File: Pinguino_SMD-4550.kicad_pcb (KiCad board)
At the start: 2 copper layers, 50.8 x 25 mm, 55 parts, among them P1 uUSB, P10 CONN_01X01, P11 CONN_01X01, P12 CONN_01X01, P13 CONN_01X01, P14 CONN_01X01, P15 CONN_01X01, P16 CONN_01X01, P17 CONN_01X01, P18 CONN_01X01, P19 CONN_01X01, P2 CONN_01X01, P20 CONN_01X01, P21 CONN_01X01, P22 CONN_01X01, P23 CONN_01X01, P24 CONN_01X01, P25 CONN_01X01, P26 CONN_01X01, P27 CONN_01X01, P28 CONN_01X01, P29 CONN_01X01, P3 CONN_01X01, P30 CONN_01X01, P31 CONN_01X01, P32 CONN_01X01, P33 CONN_01X01, P34 CONN_01X01, P35 CONN_01X01, P36 CONN_01X01, P37 CONN_01X01, P38 CONN_01X01, P4 CONN_01X01, P5 CONN_01X01, P6 CONN_01X01, P7 CONN_01X01, P8 CONN_01X01, P9 CONN_01X01, SW1 Reset, U1 PIC18(L)F4550-I/PT, Y1 Crystal

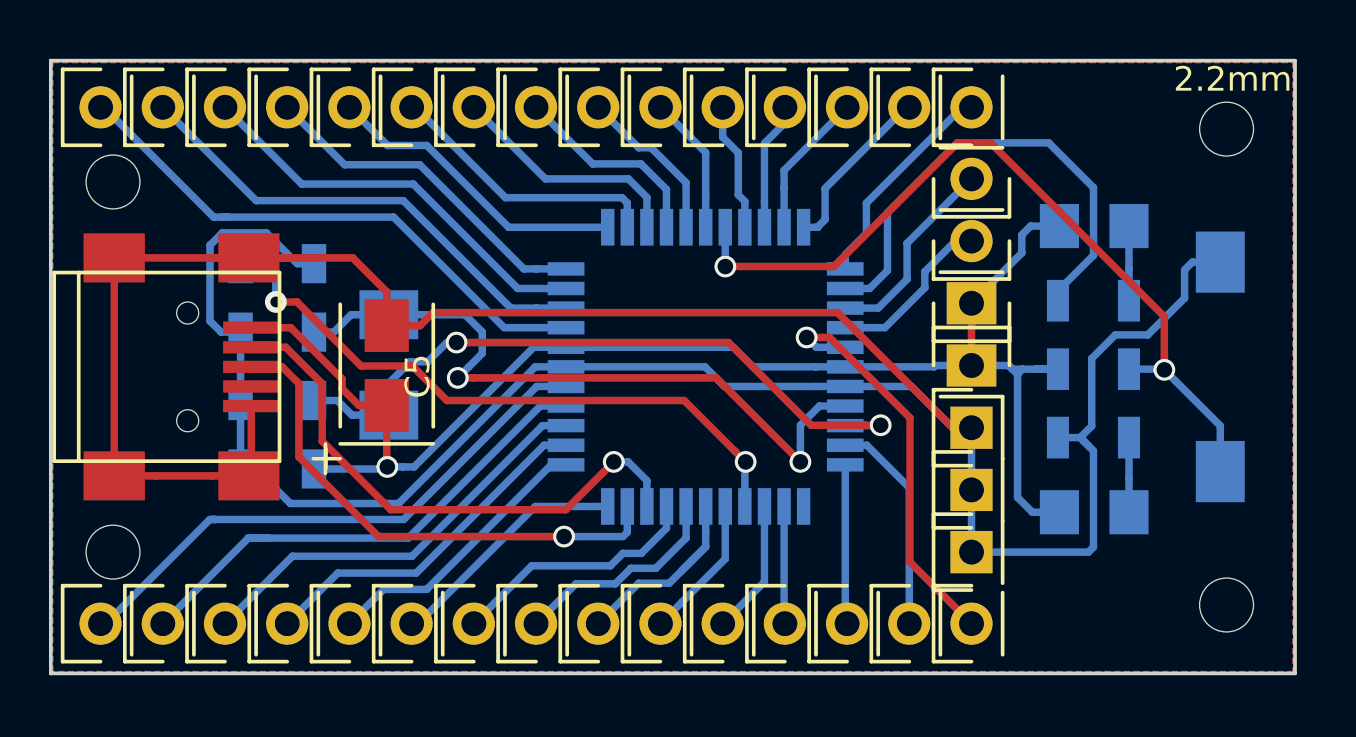
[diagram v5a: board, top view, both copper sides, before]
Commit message: Silkscreen layers
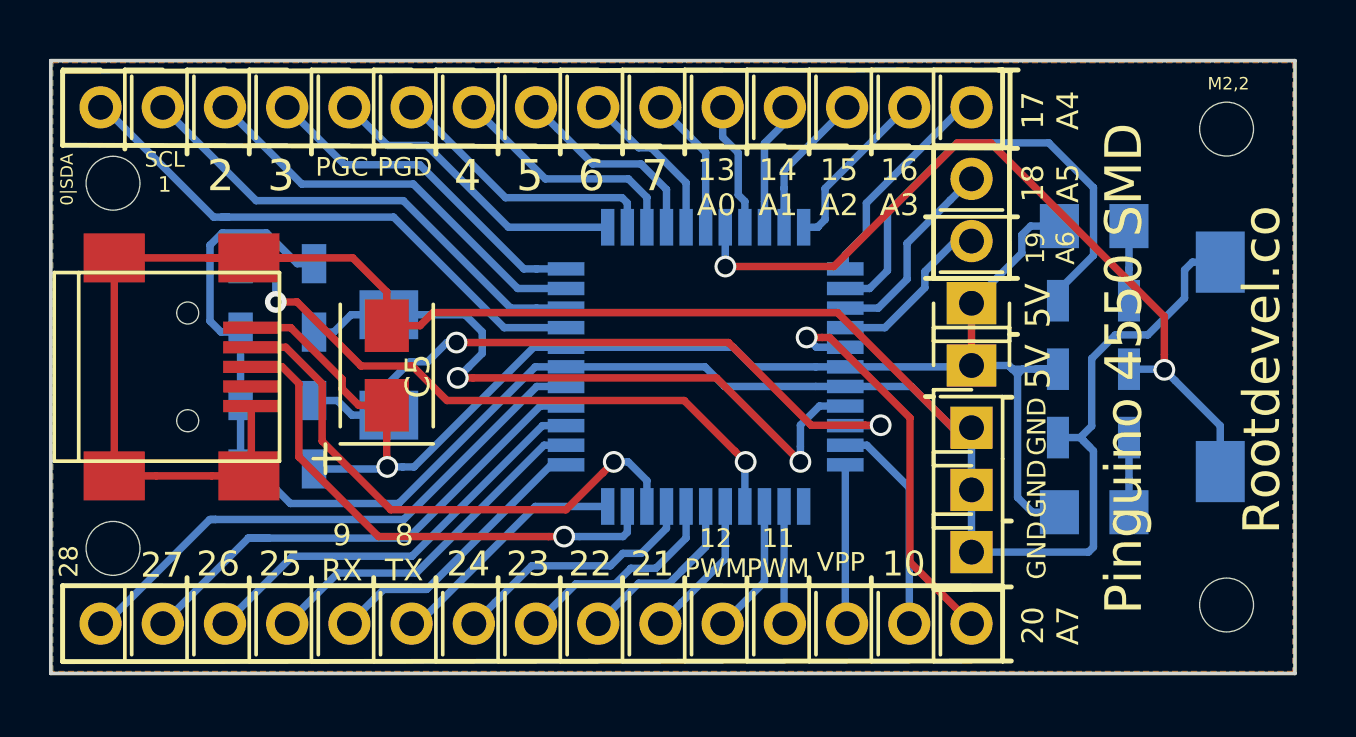
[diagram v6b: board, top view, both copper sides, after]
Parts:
- added G***: LOGO, LOGO, B.Cu at (66.9, 60.0)
- SW1: value Reset -> SW Reset
- moved REF** 0.15 mm to (66.8, 67.4)
- moved REF** 0.05 mm to (66.8, 52.5)
- renumbered 2.2mm to M2,2
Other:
- board text added: "0 SDA"
- board text added: "0|SDA"
- board text added: "1"
- board text added: "10"
- board text added: "11 PWM"
- board text added: "12 PWM"
- board text added: "13 A0"
- board text added: "14 A1"
- board text added: "15 A2"
- board text added: "16 A3"
- board text added: "17 A4"
- board text added: "18 A5"
- board text added: "19 A6"
- board text added: "19|A6"
- board text added: "2"
- board text added: "20 A7"
- board text added: "21"
- board text added: "22"
- board text added: "23"
- board text added: "24"
- board text added: "25"
- board text added: "26"
- board text added: "27"
- board text added: "28"
- board text added: "3"
- board text added: "4"
- board text added: "5"
- board text added: "5V"
- board text added: "6"
- board text added: "7"
- board text added: "8 TX"
- board text added: "9 RX"
- board text added: "GND"
- board text added: "PGC"
- board text added: "PGD"
- board text added: "Pinguino 4550 SMD"
- board text added: "Rootdevel.co"
- board text added: "SCL 1"
- board text added: "VPP"
